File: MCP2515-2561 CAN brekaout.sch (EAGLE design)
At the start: 13 parts, among them IC1 MCP2515-I-ML, IC2 PRQV8.00CR1510Y00L, IC3 PESD5V2S2UT, IC4 MCP2561-2, X1 22-23-2021

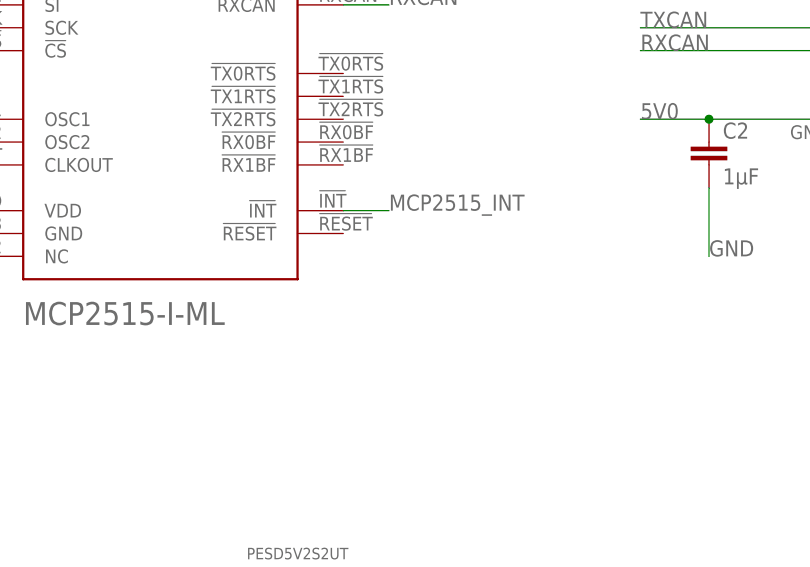
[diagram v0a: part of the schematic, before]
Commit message: - added pullup to reset pin on MCP2515-2561 CAN brekaout.brd
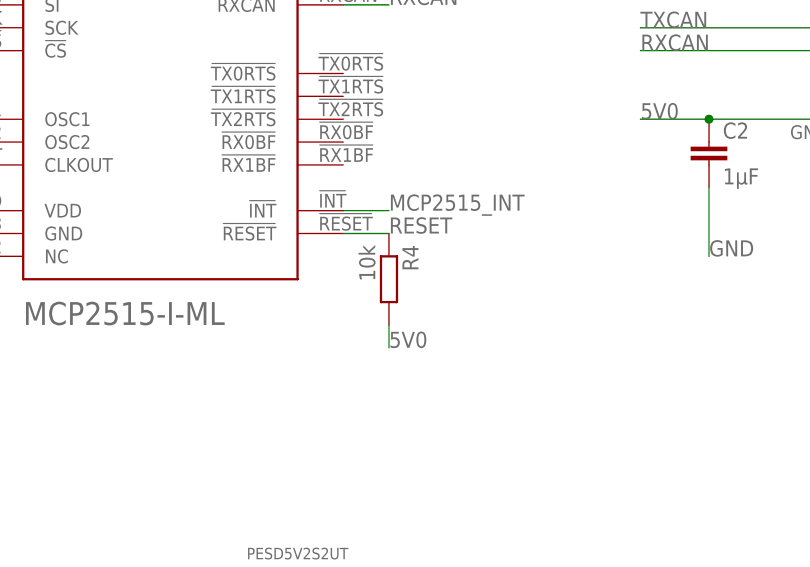
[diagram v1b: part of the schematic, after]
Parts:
- added R4: 10k, rcl:R-EU_R0402
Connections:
- new net RESET: IC1.!RESET!, R4.1
- net 5V0: now also R4.2
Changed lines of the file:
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@@
 <?xml version="1.0" encoding="utf-8"?>
 <!DOCTYPE eagle SYSTEM "eagle.dtd">
-<eagle version="9.0.0">
+<eagle version="9.0.1">
 <drawing>
 <settings>
@@
 <part name="IC3" library="PESDxS2UT" deviceset="PESDXS2UT" device="" value="PESD5V2S2UT"/>
 <part name="JP1" library="pinhead" library_urn="urn:adsk.eagle:library:325" deviceset="PINHD-1X8" device="" package3d_urn="urn:adsk.eagle:package:22409/2" value="header"/>
+<part name="R4" library="rcl" library_urn="urn:adsk.eagle:library:334" deviceset="R-EU_" device="R0402" package3d_urn="urn:adsk.eagle:package:23547/1" value="10k"/>
 </parts>
 <sheets>
@@
 <instance part="IC3" gate="G$1" x="228.6" y="-43.18" rot="R180"/>
 <instance part="JP1" gate="A" x="177.8" y="-35.56" rot="R180"/>
+<instance part="R4" gate="G$1" x="241.3" y="7.62" rot="R270"/>
 </instances>
 <busses>
@@
 <label x="190.5" y="-43.18" size="1.778" layer="95"/>
 </segment>
+<segment>
+<pinref part="R4" gate="G$1" pin="2"/>
+<wire x1="241.3" y1="2.54" x2="241.3" y2="0" width="0.1524" layer="91"/>
+<label x="241.3" y="0" size="1.778" layer="95"/>
+</segment>
 </net>
 <net name="OSC1" class="0">
@@
 </segment>
 </net>
+<net name="RESET" class="0">
+<segment>
+<pinref part="IC1" gate="G$1" pin="!RESET!"/>
+<wire x1="236.22" y1="12.7" x2="241.3" y2="12.7" width="0.1524" layer="91"/>
+<label x="241.3" y="12.7" size="1.778" layer="95"/>
+<pinref part="R4" gate="G$1" pin="1"/>
+</segment>
+</net>
